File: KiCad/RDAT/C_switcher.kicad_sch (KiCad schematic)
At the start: 0 parts

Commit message: Add data from KiCAD and review
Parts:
- added J3: USB_C_Receptacle_PowerOnly_24P, symbol Connector:USB_C_Receptacle_PowerOnly_24P
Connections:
- new net: J3.A4 (VBUS), J3.A9 (VBUS), J3.B4 (VBUS), J3.B9 (VBUS)
- new net GND: J3.A1 (GND), J3.A12 (GND), J3.B1 (GND), J3.B12 (GND), J3.S1 (SHIELD)
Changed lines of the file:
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@@
 		(rev "0")
 	)
+	(junction
+		(at 33.02 58.42)
+		(diameter 0)
+		(color 0 0 0 0)
+	)
+	(wire
+		(pts
+			(xy 29.21 58.42) (xy 33.02 58.42)
+		)
+		(stroke
+			(width 0)
+			(type default)
+		)
+	)
+	(wire
+		(pts
+			(xy 33.02 58.42) (xy 36.83 58.42)
+		)
+		(stroke
+			(width 0)
+			(type default)
+		)
+	)
+	(symbol
+		(lib_id "power:GND")
+		(at 33.02 58.42 0)
+		(unit 1)
+		(exclude_from_sim no)
+		(in_bom yes)
+		(on_board yes)
+		(dnp no)
+		(fields_autoplaced yes)
+		(property "Reference" "#PWR019"
+			(at 33.02 64.77 0)
+			(effects
+				(font
+					(size 1.27 1.27)
+				)
+				(hide yes)
+			)
+		)
+		(property "Value" "GND"
+			(at 33.02 63.5 0)
+			(effects
+				(font
+					(size 1.27 1.27)
+				)
+			)
+		)
+		(property "Footprint" ""
+			(at 33.02 58.42 0)
+			(effects
+				(font
+					(size 1.27 1.27)
+				)
+				(hide yes)
+			)
+		)
+		(property "Datasheet" ""
+			(at 33.02 58.42 0)
+			(effects
+				(font
+					(size 1.27 1.27)
+				)
+				(hide yes)
+			)
+		)
+		(property "Description" "Power symbol creates a global label with name \"GND\" , ground"
+			(at 33.02 58.42 0)
+			(effects
+				(font
+					(size 1.27 1.27)
+				)
+				(hide yes)
+			)
+		)
+		(pin "1"
+		)
+		(instances
+			(project ""
+				(path "/0db9370a-8a21-4fd2-83a9-f207c3725dc9/54b1957b-bb7d-4fff-b2e4-109cfbcf15fe"
+					(reference "#PWR019")
+					(unit 1)
+				)
+			)
+		)
+	)
+	(symbol
+		(lib_id "Connector:USB_C_Receptacle_PowerOnly_24P")
+		(at 36.83 40.64 0)
+		(unit 1)
+		(exclude_from_sim no)
+		(in_bom yes)
+		(on_board yes)
+		(dnp no)
+		(fields_autoplaced yes)
+		(property "Reference" "J3"
+			(at 36.83 22.86 0)
+			(effects
+				(font
+					(size 1.27 1.27)
+				)
+			)
+		)
+		(property "Value" "USB_C_Receptacle_PowerOnly_24P"
+			(at 36.83 25.4 0)
+			(effects
+				(font
+					(size 1.27 1.27)
+				)
+			)
+		)
+		(property "Footprint" ""
+			(at 40.64 38.1 0)
+			(effects
+				(font
+					(size 1.27 1.27)
+				)
+				(hide yes)
+			)
+		)
+		(property "Datasheet" "https://www.usb.org/sites/default/files/documents/usb_type-c.zip"
+			(at 36.83 40.64 0)
+			(effects
+				(font
+					(size 1.27 1.27)
+				)
+				(hide yes)
+			)
+		)
+		(property "Description" "USB Power-Only 24P Type-C Receptacle connector"
+			(at 36.83 40.64 0)
+			(effects
+				(font
+					(size 1.27 1.27)
+				)
+				(hide yes)
+			)
+		)
+		(pin "A12"
+		)
+		(pin "B12"
+		)
+		(pin "B9"
+		)
+		(pin "S1"
+		)
+		(pin "B4"
+		)
+		(pin "A9"
+		)
+		(pin "A5"
+		)
+		(pin "A4"
+		)
+		(pin "B1"
+		)
+		(pin "A1"
+		)
+		(pin "B5"
+		)
+		(instances
+			(project ""
+				(path "/0db9370a-8a21-4fd2-83a9-f207c3725dc9/54b1957b-bb7d-4fff-b2e4-109cfbcf15fe"
+					(reference "J3")
+					(unit 1)
+				)
+			)
+		)
+	)
 )

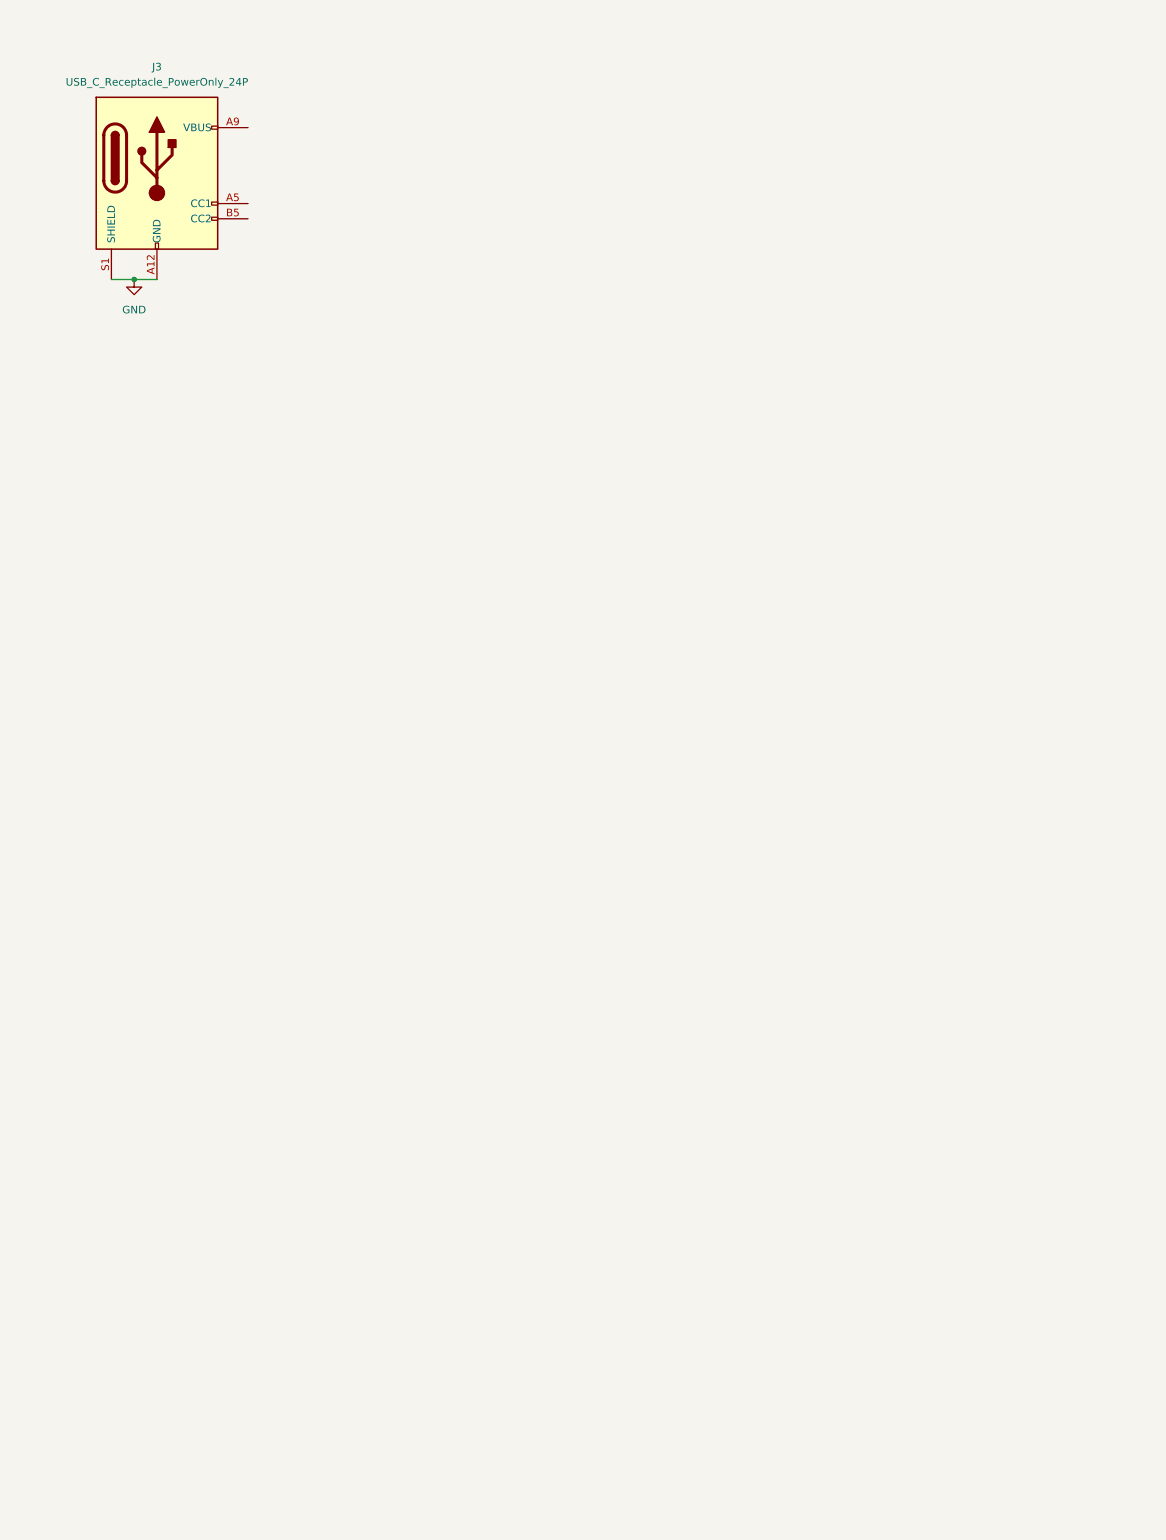
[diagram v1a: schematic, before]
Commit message: Added kicad USBC controller and connected VBUS
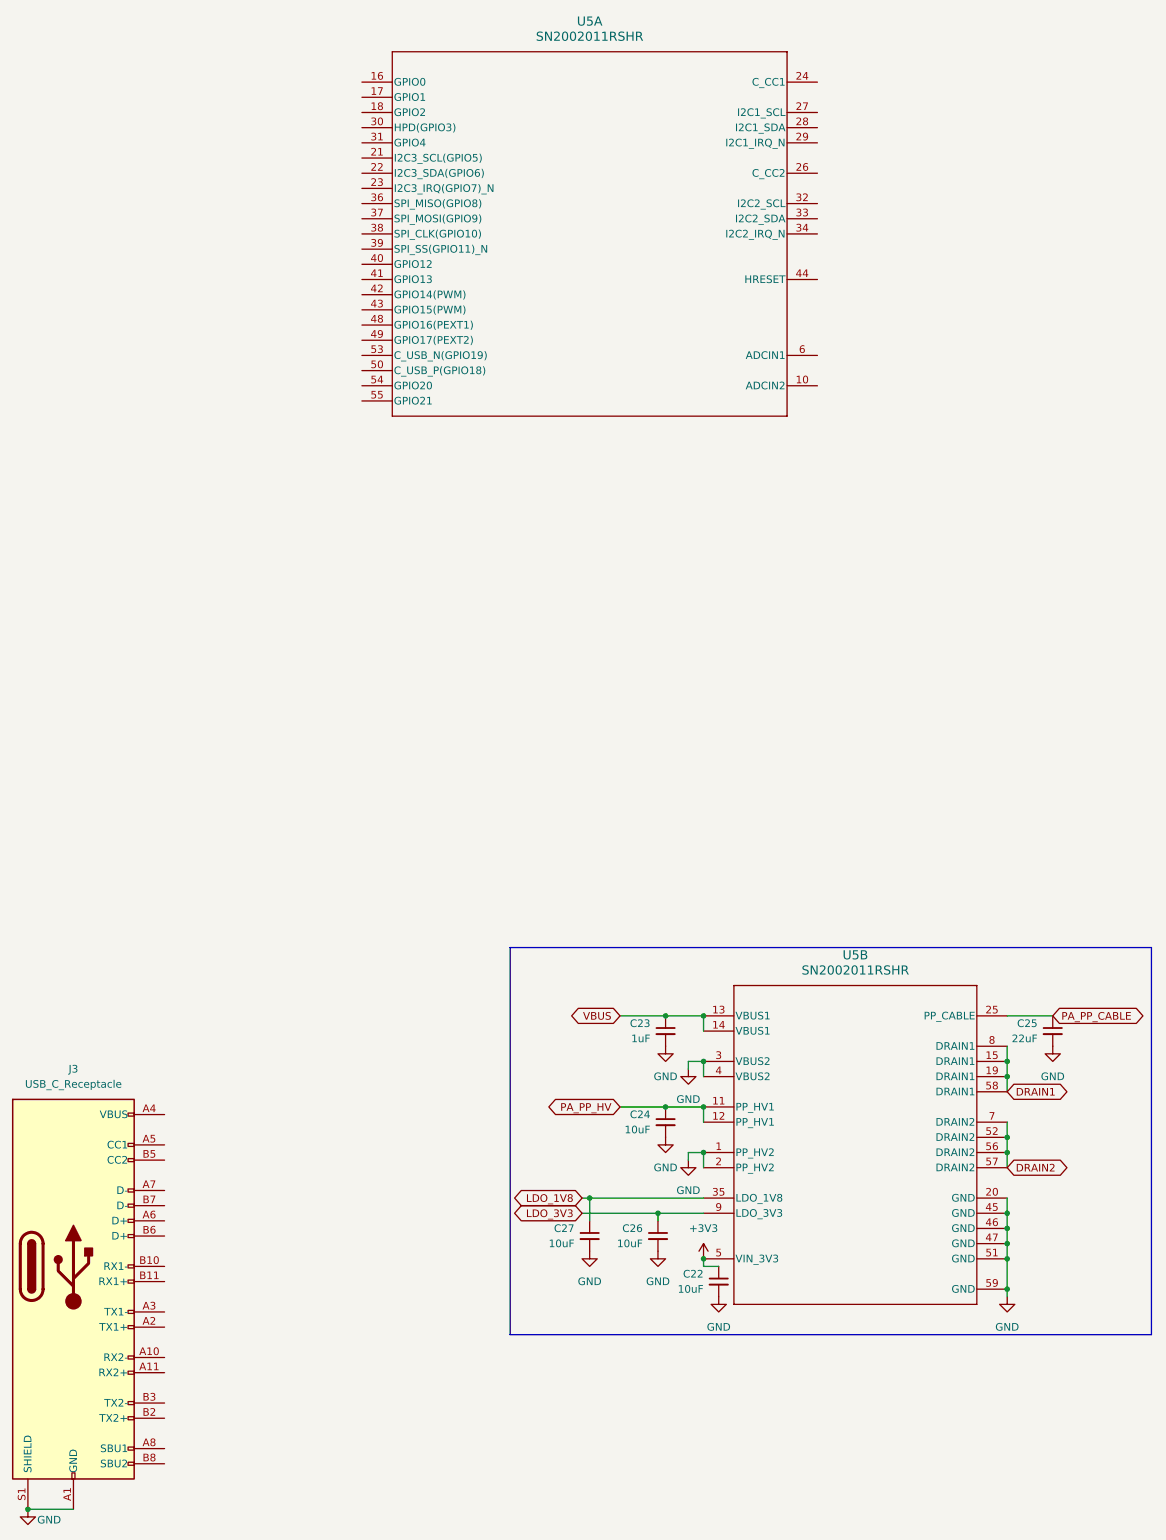
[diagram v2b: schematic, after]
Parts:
- removed J3: USB_C_Receptacle_PowerOnly_24P, symbol Connector:USB_C_Receptacle_PowerOnly_24P
- added C22, C24, C26, C27: 10uF, symbol Device:C_Small
- added C23: 1uF, symbol Device:C_Small
- added C25: 22uF, symbol Device:C_Small
- added J3: USB_C_Receptacle, symbol Connector:USB_C_Receptacle
- added U5: SN2002011RSHR, RSH0056E-MFG, symbol TPS65987DDK:SN2002011RSHR
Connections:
- net GND: now also C22.2, C23.2, C24.2, C25.2, C26.2, C27.2, J3.A1 (GND), J3.A12 (GND), J3.B1 (GND), J3.B12 (GND), J3.S1 (SHIELD), U5.1 (PP_HV2), U5.2 (PP_HV2), U5.20 (GND), U5.3 (VBUS2), U5.4 (VBUS2), U5.45 (GND), U5.46 (GND), U5.47 (GND), U5.51 (GND), U5.59 (GND)
- new net: J3.A4 (VBUS), J3.A9 (VBUS), J3.B4 (VBUS), J3.B9 (VBUS)
- new net +3V3: C22.1, U5.5 (VIN_3V3)
- new net DRAIN1: U5.15 (DRAIN1), U5.19 (DRAIN1), U5.58 (DRAIN1), U5.8 (DRAIN1)
- new net DRAIN2: U5.52 (DRAIN2), U5.56 (DRAIN2), U5.57 (DRAIN2), U5.7 (DRAIN2)
- new net LDO_1V8: C27.1, U5.35 (LDO_1V8)
- new net LDO_3V3: C26.1, U5.9 (LDO_3V3)
- new net PA_PP_CABLE: C25.1, U5.25 (PP_CABLE)
- new net PA_PP_HV: C24.1, U5.11 (PP_HV1), U5.12 (PP_HV1)
- new net VBUS: C23.1, U5.13 (VBUS1), U5.14 (VBUS1)

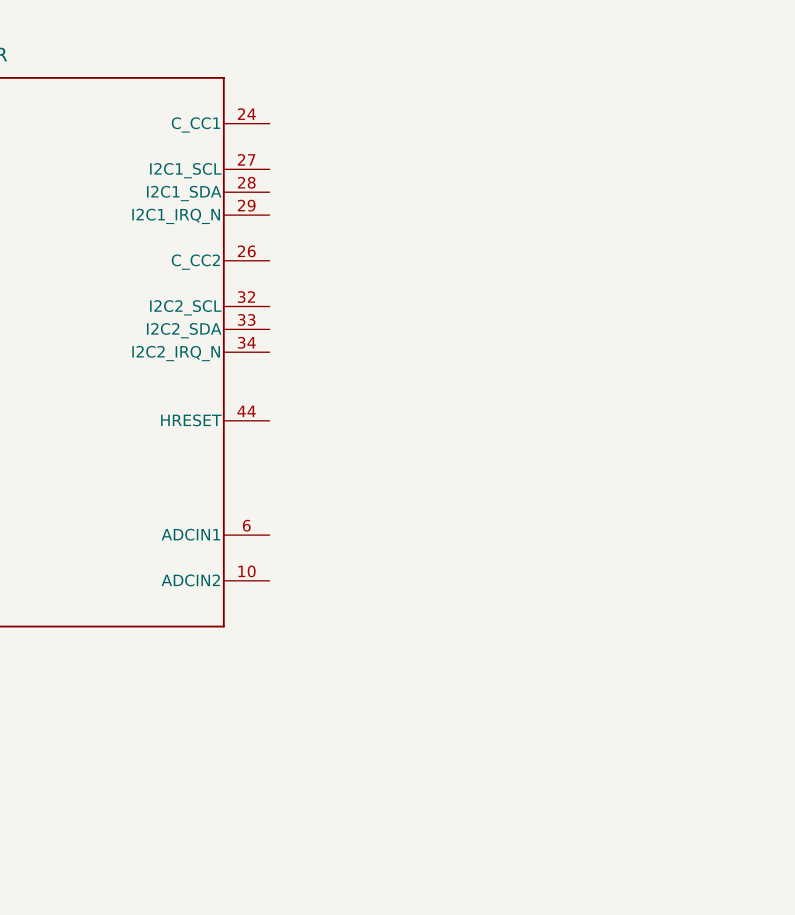
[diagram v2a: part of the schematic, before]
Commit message: tb4 prooved to be too diffucult/expensive...
Issue: would cost $200+ to devlop for this chipset
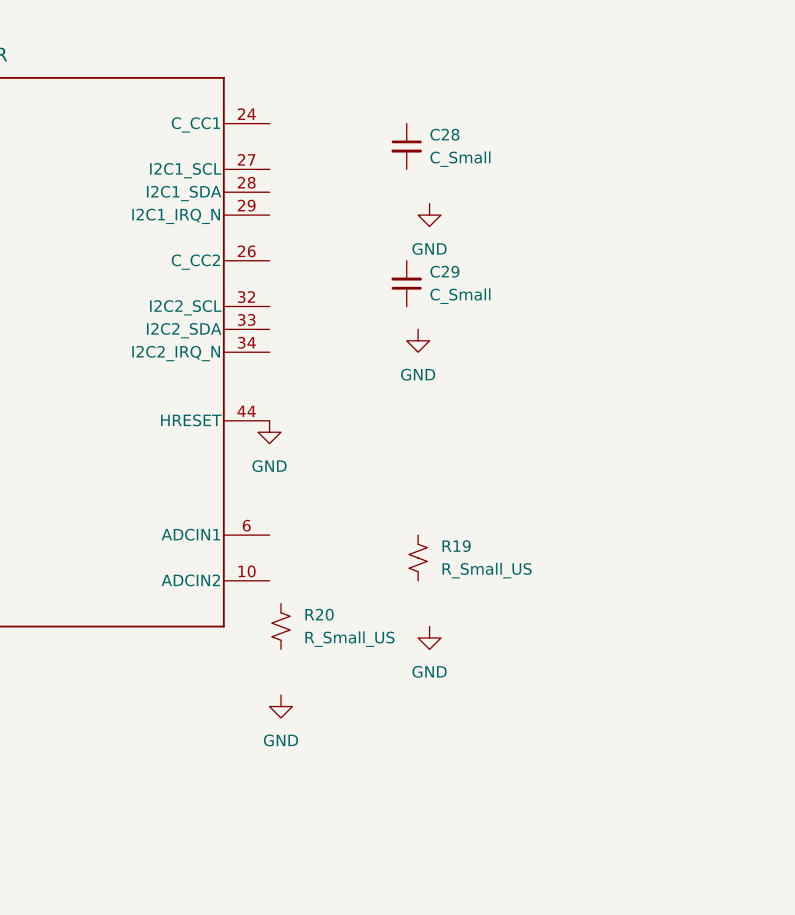
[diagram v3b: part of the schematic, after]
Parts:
- added C28, C29: C_Small, symbol Device:C_Small
- added R19, R20: R_Small_US, symbol Device:R_Small_US
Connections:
- net GND: now also U5.44 (HRESET)

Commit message: Update BMS
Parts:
- removed U5: SN2002011RSHR, RSH0056E-MFG, symbol TPS65987DDK:SN2002011RSHR
- added C30: 10uF, symbol Device:C_Small
- added C31: 1uF, symbol Device:C_Small
- added C32: 100nF, symbol Device:C_Small
- added D108: D_TVS, symbol Device:D_TVS
- added D109, D110: GREEN, symbol Device:LED
- added F1: Fuse_Small, symbol Device:Fuse_Small
- added MOSFET1: BSC009NE2LS5ATMA1, PG-TDSON-8-1_INF, symbol BSC009NE2LS5ATMA1:BSC009NE2LS5ATMA1
- added R21, R27: 10k, symbol Device:R_Small_US
- added R23, R31: 100k, symbol Device:R_Small_US
- added R25, R26: 5.1k, symbol Device:R_Small_US
- added R28, R29: 1k, symbol Device:R_Small_US
- added TP10, TP11, TP12: TestPoint_Small, symbol Connector:TestPoint_Small
- added U6: PTPS25751DREFR, WQFN38_REF_TEX, symbol TPS25751:PTPS25751DREFR
- C22: value 10uF -> 1uF
- C25: value 22uF -> 10uF
- C27: value 10uF -> 100nF
- C28: value C_Small -> 100nF
- C29: value C_Small -> 10uF
- R19: value R_Small_US -> 47.5k
- R20: value R_Small_US -> 10k
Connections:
- net +3V3 is gone; now on net LDO_3V3: C22.1
- net LDO_1V8 is gone; now on net CC1: C27.1
- net GND: now also C26.1, C28.2, C29.1, R20.1, C30.1, C31.1, D108.2 (A2), D109.1 (K), D110.1 (K), R21.1, R25.2, R26.2, R27.2, R31.1, U6.11 (GND), U6.12 (GND), U6.14 (GND), U6.31 (GND), U6.39 (GND); no longer C26.2
- net LDO_3V3: now also R19.2, R23.2, U6.1 (LDO_3V3); no longer C26.1
- net at J3.A4 (VBUS), J3.A9 (VBUS), J3.B4 (VBUS)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: now also F1.1
- net CC1: now reaches J3.A5 (CC1)
- net CC1: now also R25.1, U6.28 (CC1)
- net CC2: now reaches J3.B5 (CC2)
- net CC2: now also C28.1, R26.1, U6.29 (CC2)
- net ADC_IN_1: now reaches R19.1
- net ADC_IN_1: now also R21.2, U6.2 (ADCIN1)
- net ADC_IN_2: now reaches R20.2
- net ADC_IN_2: now also R23.1, U6.3 (ADCIN2)
- net at C29.2: now also U6.32 (VBUS), U6.33 (VBUS)
- net PA_PP_CABLE renamed POWER CHARGER OUTPUT
- net POWER CHARGER OUTPUT: now also R29.2, TP11.1, U6.20 (PPHV), U6.21 (PPHV), U6.22 (PPHV)
- net PA_PP_HV renamed DRAIN
- net DRAIN: now also C26.2, D108.1 (A1), MOSFET1.5, MOSFET1.6, MOSFET1.7, MOSFET1.8, R28.2, R31.2, TP10.1, U6.15 (DRAIN), U6.23 (VBUS_IN), U6.24 (VBUS_IN), U6.25 (VBUS_IN), U6.30 (DRAIN), U6.40 (DRAIN)
- net VBUS renamed LDO_1V5
- net LDO_1V5: now also U6.4 (LDO_1V5)
- new net: C32.2, MOSFET1.4, R27.1, TP12.1
- new net: D109.2 (A), R28.1
- new net: D110.2 (A), R29.1
- new net: C30.2, U6.34 (PP5V), U6.35 (PP5V)
- new net Filter_Mos: C32.1, F1.2, MOSFET1.1, MOSFET1.2, MOSFET1.3
- new net VIN_3V3: C31.2, U6.38 (VIN_3V3)
- no-connect marks 0 -> 14
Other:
- note added: "Drain"
- note added: "Gate"
- note added: "source"
